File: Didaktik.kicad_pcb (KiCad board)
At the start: 2 copper layers, 209.6 x 76.2 mm, 129 parts, among them J1 Conn_01x04_MountingPin, J2 AVR-ISP-6, J3 Conn_01x03, Q1 2N2222, SW1 SW_Push_45deg, SW10 SW_Push_45deg, SW11 SW_Push_45deg, SW12 SW_Push_45deg, SW13 SW_Push_45deg, SW14 SW_Push_45deg, SW15 SW_Push_45deg, SW16 SW_Push_45deg, SW17 SW_Push_45deg, SW18 SW_Push_45deg, SW19 SW_Push_45deg, SW2 SW_Push_45deg, SW20 SW_Push_45deg, SW21 SW_Push_45deg, SW22 SW_Push_45deg, SW23 SW_Push_45deg, SW24 SW_Push_45deg, SW25 SW_Push_45deg, SW26 SW_Push_45deg, SW27 SW_Push_45deg, SW28 SW_Push_45deg, SW29 SW_Push_45deg, SW3 SW_Push_45deg, SW30 SW_Push_45deg, SW31 SW_Push_45deg, SW31a1 SW_Push_45deg, SW32 SW_Push_45deg, SW32a1 SW_Push_45deg, SW33 SW_Push_45deg, SW33a1 SW_Push_45deg, SW34 SW_Push_45deg, SW34a1 SW_Push_45deg, SW34b1 SW_Push_45deg, SW35 SW_Push_45deg, SW35a1 SW_Push_45deg, SW35b1 SW_Push_45deg, SW35c1 SW_Push_45deg, SW36 SW_Push_45deg, SW36a1 SW_Push_45deg, SW36b1 SW_Push_45deg, SW36c1 SW_Push_45deg, SW37 SW_Push_45deg, SW37a1 SW_Push_45deg, SW37b1 SW_Push_45deg, SW38 SW_Push_45deg, SW38a1 SW_Push_45deg, SW39 SW_Push_45deg, SW39a1 SW_Push_45deg, SW4 SW_Push_45deg, SW40 SW_Push_45deg, SW40a1 SW_Push_45deg, SW41 RotaryEncoder_Switch, SW42 RotaryEncoder_Switch, SW5 SW_Push_45deg, SW6 SW_Push_45deg, SW7 SW_Push_45deg, SW8 SW_Push_45deg, SW9 SW_Push_45deg, U1 ATmega32U4-M, Y1 Crystal_GND24_Small

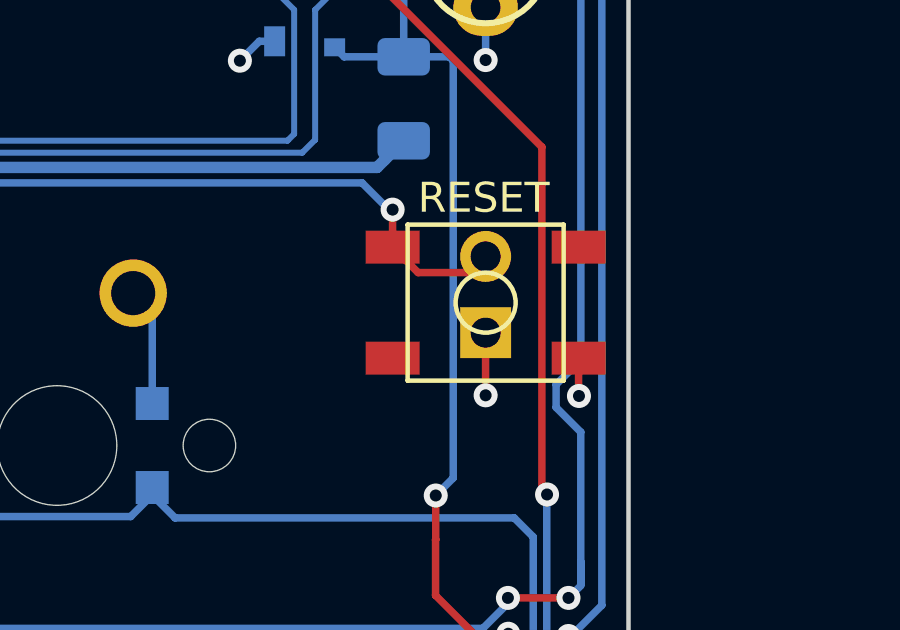
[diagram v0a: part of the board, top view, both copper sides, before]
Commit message: updated BOM with correct parts
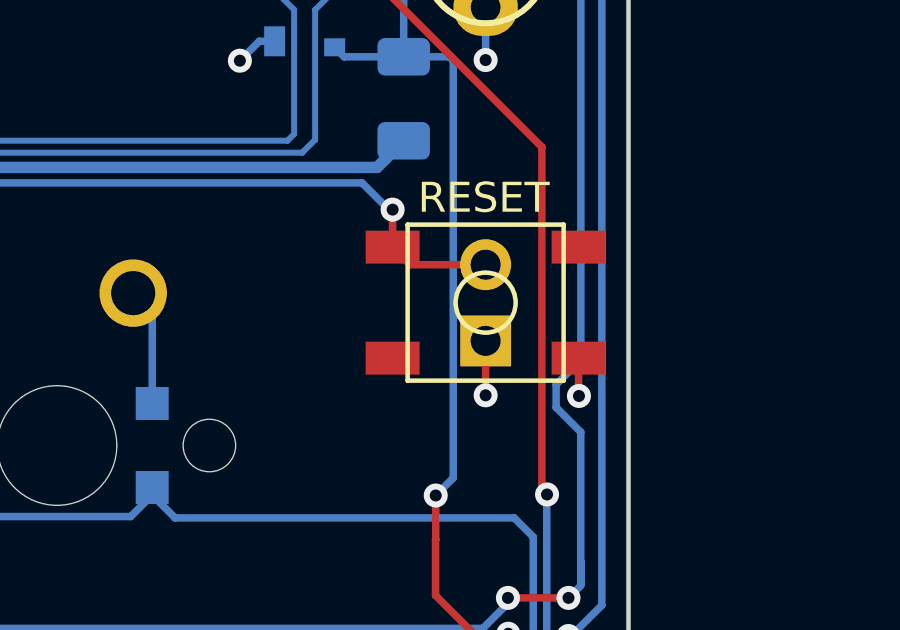
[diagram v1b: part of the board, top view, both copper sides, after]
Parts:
- moved SW_Reset2 0.27 mm to (236.5, 56.8)
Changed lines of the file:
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@@
   )
   (footprint "Connector_PinHeader_2.54mm:PinHeader_1x02_P2.54mm_Vertical" (layer "B.Cu")
-    (at 236.5375 56.5625)
+    (at 236.5375 56.8375)
     (descr "Through hole straight pin header, 1x02, 2.54mm pitch, single row")
     (tags "Through hole pin header THT 1x02 2.54mm single row")
@@
     (property "ki_description" "Push button switch, generic, two pins")
     (property "ki_keywords" "switch normally-open pushbutton push-button")
-    (attr through_hole)
+    (attr through_hole exclude_from_pos_files exclude_from_bom)
     (fp_text reference "SW_Reset2" (at 0 2.33 180) (layer "B.SilkS")
         (effects (font (size 1 1) (thickness 0.15)) (justify mirror))
@@
   (segment (start 240.411 39.251926) (end 240.411 65.650412) (width 0.25) (layer "B.Cu") (net 53))
   (segment (start 239.6375 57.4125) (end 239.6375 58.6625) (width 0.25) (layer "F.Cu") (net 54))
-  (segment (start 236.5375 56.5625) (end 236.5375 58.651931) (width 0.25) (layer "F.Cu") (net 54))
+  (segment (start 236.5375 58.651931) (end 236.5375 56.8375) (width 0.25) (layer "F.Cu") (net 54))
   (segment (start 239.6375 58.6625) (end 239.649 58.674) (width 0.25) (layer "F.Cu") (net 54))
   (via (at 41.275 47.117) (size 0.8) (drill 0.4) (layers "F.Cu" "B.Cu") (net 54))
@@
   (segment (start 82.55 42.925) (end 83.268901 43.643901) (width 0.25) (layer "B.Cu") (net 71))
   (segment (start 55.79002 67.774) (end 52.14627 71.41775) (width 0.25) (layer "B.Cu") (net 71))
+  (segment (start 234.0225 54.2975) (end 236.5375 54.2975) (width 0.25) (layer "F.Cu") (net 72))
   (segment (start 233.4375 53.7125) (end 233.4375 52.4625) (width 0.25) (layer "F.Cu") (net 72))
-  (segment (start 233.4375 53.7125) (end 234.2875 54.5625) (width 0.25) (layer "F.Cu") (net 72))
   (segment (start 36.957 52.098) (end 36.957 59.817) (width 0.25) (layer "F.Cu") (net 72))
-  (segment (start 234.2875 54.5625) (end 236.5375 54.5625) (width 0.25) (layer "F.Cu") (net 72))
+  (segment (start 233.4375 53.7125) (end 234.0225 54.2975) (width 0.25) (layer "F.Cu") (net 72))
   (via (at 36.957 52.098) (size 0.8) (drill 0.4) (layers "F.Cu" "B.Cu") (net 72))
   (via (at 233.4375 52.4625) (size 0.8) (drill 0.4) (layers "F.Cu" "B.Cu") (net 72))

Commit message: added STEM project WIP
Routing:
- net VCC: track 261.1 -> 260.5 mm
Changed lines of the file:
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@@
   (segment (start 231.822 47.368) (end 231.505 47.051) (width 0.25) (layer "B.Cu") (net 62))
   (segment (start 225.425 82.5405) (end 225.425 82.55) (width 0.25) (layer "B.Cu") (net 62))
-  (segment (start 233.807 47.368) (end 235.328 47.368) (width 0.25) (layer "B.Cu") (net 62))
   (segment (start 229.625 35.975) (end 229.6735 35.975) (width 0.25) (layer "B.Cu") (net 62))
-  (segment (start 235.331 47.371) (end 235.458 47.498) (width 0.25) (layer "B.Cu") (net 62))
   (segment (start 229.625 39.2875) (end 229.625 35.975) (width 0.25) (layer "B.Cu") (net 62))
   (segment (start 225.425 84.4395) (end 225.1505 84.165) (width 0.25) (layer "B.Cu") (net 62))
   (segment (start 62.253 89.789) (end 62.253 84.559) (width 0.25) (layer "B.Cu") (net 62))
+  (segment (start 233.807 47.368) (end 234.95 47.368) (width 0.25) (layer "B.Cu") (net 62))
   (segment (start 225.425 82.55) (end 225.679 82.804) (width 0.25) (layer "B.Cu") (net 62))
-  (segment (start 235.458 61.407655) (end 235.458 47.498) (width 0.25) (layer "B.Cu") (net 62))
-  (segment (start 234.874569 61.991086) (end 235.458 61.407655) (width 0.25) (layer "B.Cu") (net 62))
+  (segment (start 234.95 47.368) (end 235.007 47.425) (width 0.25) (layer "B.Cu") (net 62))
+  (segment (start 235.007 61.858655) (end 234.874569 61.991086) (width 0.25) (layer "B.Cu") (net 62))
   (segment (start 225.1505 84.165) (end 62.829 84.165) (width 0.25) (layer "B.Cu") (net 62))
   (segment (start 62.647 84.165) (end 62.829 84.165) (width 0.25) (layer "B.Cu") (net 62))
   (segment (start 229.9375 39.6) (end 229.625 39.2875) (width 0.25) (layer "B.Cu") (net 62))
-  (segment (start 235.328 47.368) (end 235.331 47.371) (width 0.25) (layer "B.Cu") (net 62))
   (segment (start 237.363 82.804) (end 237.617 82.55) (width 0.25) (layer "B.Cu") (net 62))
   (segment (start 229.9615 35.687) (end 233.1365 35.687) (width 0.25) (layer "B.Cu") (net 62))
@@
   (segment (start 225.679 82.804) (end 237.363 82.804) (width 0.25) (layer "B.Cu") (net 62))
   (segment (start 229.6735 35.975) (end 229.9615 35.687) (width 0.25) (layer "B.Cu") (net 62))
+  (segment (start 235.007 47.425) (end 235.007 61.858655) (width 0.25) (layer "B.Cu") (net 62))
   (segment (start 233.807 47.368) (end 233.807 36.3575) (width 0.25) (layer "B.Cu") (net 62))
   (segment (start 62.253 84.559) (end 62.647 84.165) (width 0.25) (layer "B.Cu") (net 62))
